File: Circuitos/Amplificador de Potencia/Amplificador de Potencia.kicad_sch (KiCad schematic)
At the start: 110 parts, among them Q1 NPN, Q1 PNP, Q10 PNP, Q11 NPN, Q12 PNP, Q13 NPN, Q14 PNP, Q15 NPN, Q16 PNP, Q17 NPN, Q18 PNP, Q19 PNP, Q2 NPN, Q20 NPN, Q3 NPN, Q4 PNP, Q5 NPN, Q6 PNP, Q7 NPN, Q8 PNP, Q9 NPN, U1 ${SIM.PARAMS}, U10 ${SIM.PARAMS}, U11 ${SIM.PARAMS}, U2 ${SIM.PARAMS}, U3 ${SIM.PARAMS}, U4 ${SIM.PARAMS}, U5 ${SIM.PARAMS}, U6 ${SIM.PARAMS}, U7 ${SIM.PARAMS}, U8 ${SIM.PARAMS}, U9 ${SIM.PARAMS}

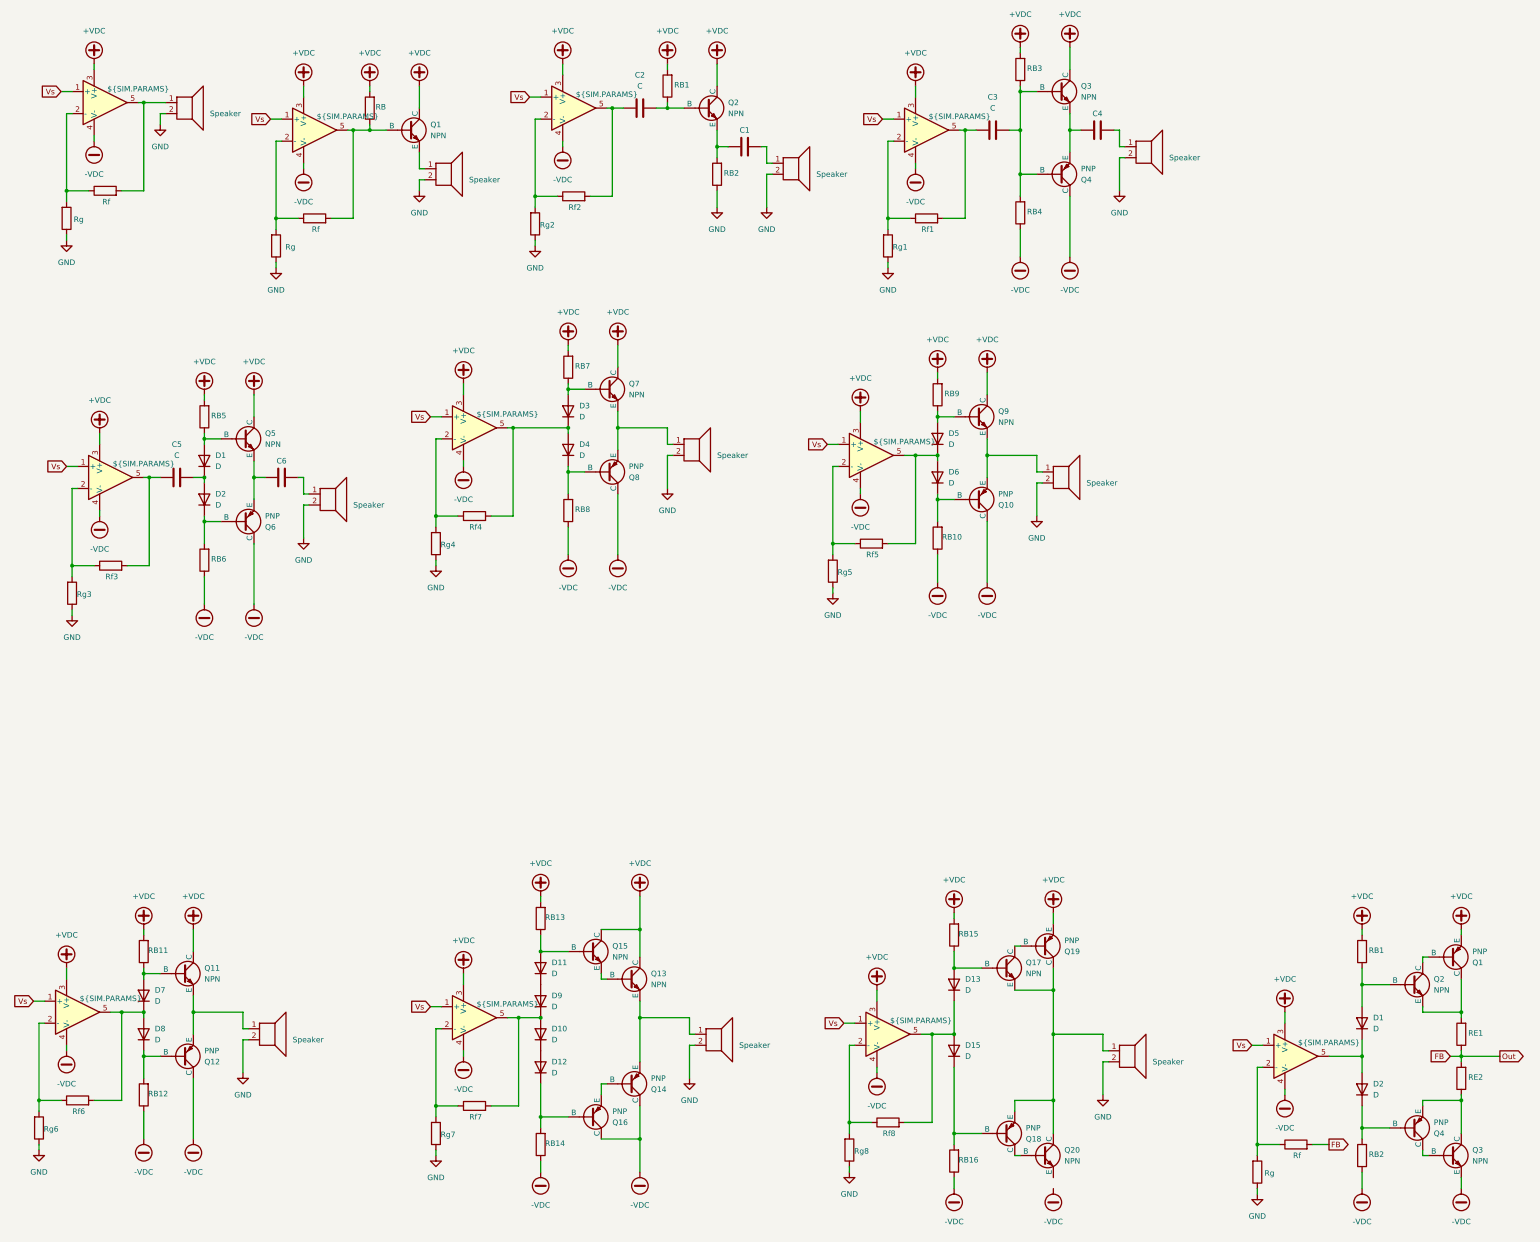
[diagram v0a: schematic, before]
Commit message: Correcciones pequeñas y eliminación duplicados
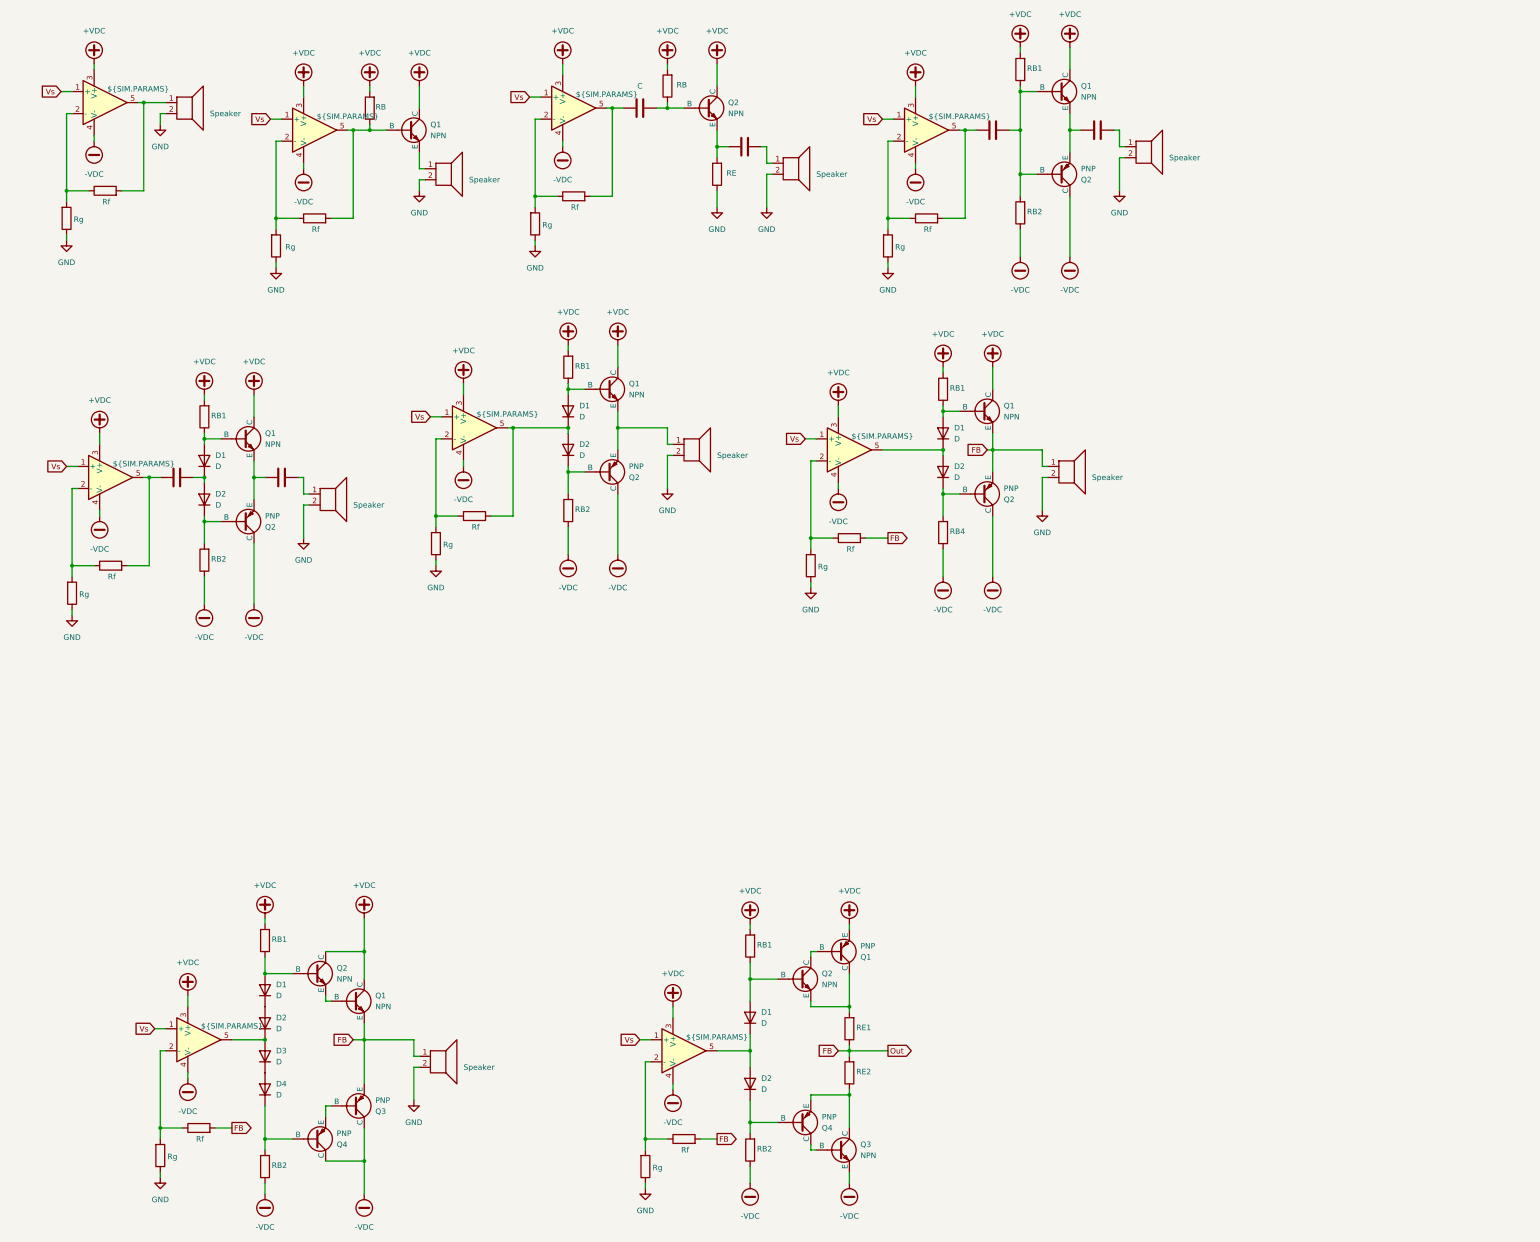
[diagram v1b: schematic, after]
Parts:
- removed D13, D15, D5, D6, D7, D8: D, symbol Device:D
- removed LS10, LS8: Speaker, symbol Device:Speaker
- removed Q10, Q12, Q18, Q19: PNP, symbol Simulation_SPICE:PNP
- removed Q11, Q17, Q20, Q9: NPN, symbol Simulation_SPICE:NPN
- removed RB10, RB11, RB12, RB15, RB16, RB9, Rf5, Rf6, Rf8, Rg5, Rg6, Rg8: ~, symbol Device:R
- removed U10, U8: ${SIM.PARAMS}, symbol Simulation_SPICE:OPAMP
- added D1, D2: D, symbol Device:D
- added Q1: NPN, symbol Simulation_SPICE:NPN
- added Q2: PNP, symbol Simulation_SPICE:PNP
- added RB1, RB4, Rf, Rg: ~, symbol Device:R
- renumbered D11 to D1, D3 to D1, D9 to D2, D4 to D2, D10 to D3, D12 to D4, Q3 to Q1, Q13 to Q1, Q7 to Q1, Q5 to Q1, Q8 to Q2, Q4 to Q2, Q15 to Q2, Q6 to Q2, Q14 to Q3, Q16 to Q4, RB1 to RB, RB3 to RB1, RB7 to RB1, RB5 to RB1, RB13 to RB1, RB4 to RB2, RB14 to RB2, RB6 to RB2, RB8 to RB2, RB2 to RE, Rf3 to Rf, Rf2 to Rf, Rf4 to Rf, Rf7 to Rf, Rf1 to Rf, Rg7 to Rg, Rg2 to Rg, Rg1 to Rg, Rg3 to Rg, Rg4 to Rg
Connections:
- net +VDC: now also Q1.1 (C), RB1.2
- net -VDC: now also Q2.1 (C), RB4.1
- net FB: now also LS7.1, LS9.1, Q1.3 (E), Q3.3 (E), Rf.2, Q1.3 (E), Q2.3 (E), Rf.2
- net GND: now also Rg.1
- net at U7.2 (-): now also Rf.1, Rg.2
- net at D2.1 (K), D3.2 (A), U9.5: no longer Rf.2
- net at U7.5: now also D1.1 (K), D2.2 (A)
- new net: D2.1 (K), Q2.2 (B), RB4.2
- new net: D1.2 (A), Q1.2 (B), RB1.1
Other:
- moved on the sheet: D1, D2, D3, D4, Q1, Q2, Q3, Q4, RB1, RB2, RE1, RE2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
